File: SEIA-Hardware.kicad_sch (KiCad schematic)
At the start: 1 part, among them IC1 MIMXRT1062DVL6A

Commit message: update 3.10
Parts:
- added IC2: BMF055, BMF055, symbol SEIA_SpecLib:BMF055

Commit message: update on pcb
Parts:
- added IC3: TLV70433DBVEVM-712, SOT95P280X145-5N, symbol SEIA_SpecLib:TLV70433DBVEVM-712
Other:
- note added: "Power"
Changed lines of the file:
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@@
+	)
+	(rectangle
+		(start 29.21 323.85)
+		(end 269.24 393.7)
+		(stroke
+			(width 0.5)
+			(type solid)
+			(color 215 255 101 1)
+		)
+		(fill
+			(type none)
+		)
 	)
 	(rectangle
@@
 		(fill
 			(type none)
+		)
+	)
+	(text "Power"
+		(exclude_from_sim no)
+		(at 39.624 400.05 0)
+		(effects
+			(font
+				(face "Mononoki Nerd Font")
+				(size 5 5)
+			)
 		)
 	)
@@
 					(unit 1)
 				)
+			)
+		)
+	)
+	(symbol
+		(lib_id "SEIA_SpecLib:TLV70433DBVEVM-712")
+		(at 57.15 345.44 0)
+		(unit 1)
+		(exclude_from_sim no)
+		(in_bom yes)
+		(on_board yes)
+		(dnp no)
+		(fields_autoplaced yes)
+		(property "Reference" "IC3"
+			(at 71.12 337.82 0)
+			(effects
+				(font
+					(size 1.27 1.27)
+				)
+			)
+		)
+		(property "Value" "TLV70433DBVEVM-712"
+			(at 71.12 340.36 0)
+			(effects
+				(font
+					(size 1.27 1.27)
+				)
+			)
+		)
+		(property "Footprint" "SOT95P280X145-5N"
+			(at 81.28 342.9 0)
+			(effects
+				(font
+					(size 1.27 1.27)
+				)
+				(justify left)
+				(hide yes)
+			)
+		)
+		(property "Datasheet" "https://componentsearchengine.com/Datasheets/5/TLV70433DBVEVM-712.pdf"
+			(at 81.28 345.44 0)
+			(effects
+				(font
+					(size 1.27 1.27)
+				)
+				(justify left)
+				(hide yes)
+			)
+		)
+		(property "Description" "TEXAS INSTRUMENTS - TLV70433DBVEVM-712 - EVALUATION BOARD, 3.3V, 150mA LDO VOLTAGE REGULATOR"
+			(at 57.15 345.44 0)
+			(effects
+				(font
+					(size 1.27 1.27)
+				)
+				(hide yes)
+			)
+		)
+		(property "Description_1" "TEXAS INSTRUMENTS - TLV70433DBVEVM-712 - EVALUATION BOARD, 3.3V, 150mA LDO VOLTAGE REGULATOR"
+			(at 81.28 347.98 0)
+			(effects
+				(font
+					(size 1.27 1.27)
+				)
+				(justify left)
+				(hide yes)
+			)
+		)
+		(property "Height" "1.45"
+			(at 81.28 350.52 0)
+			(effects
+				(font
+					(size 1.27 1.27)
+				)
+				(justify left)
+				(hide yes)
+			)
+		)
+		(property "Manufacturer_Name" "Texas Instruments"
+			(at 81.28 353.06 0)
+			(effects
+				(font
+					(size 1.27 1.27)
+				)
+				(justify left)
+				(hide yes)
+			)
+		)
+		(property "Manufacturer_Part_Number" "TLV70433DBVEVM-712"
+			(at 81.28 355.6 0)
+			(effects
+				(font
+					(size 1.27 1.27)
+				)
+				(justify left)
+				(hide yes)
+			)
+		)
+		(property "Mouser Part Number" "595-LV70433DBVEVM712"
+			(at 81.28 358.14 0)
+			(effects
+				(font
+					(size 1.27 1.27)
+				)
+				(justify left)
+				(hide yes)
+			)
+		)
+		(property "Mouser Price/Stock" "https://www.mouser.co.uk/ProductDetail/Texas-Instruments/TLV70433DBVEVM-712?qs=TeC8nwD7mVofZYBqOoN1WA%3D%3D"
+			(at 81.28 360.68 0)
+			(effects
+				(font
+					(size 1.27 1.27)
+				)
+				(justify left)
+				(hide yes)
+			)
+		)
+		(property "Arrow Part Number" "TLV70433DBVEVM-712"
+			(at 81.28 363.22 0)
+			(effects
+				(font
+					(size 1.27 1.27)
+				)
+				(justify left)
+				(hide yes)
+			)
+		)
+		(property "Arrow Price/Stock" "null?region=nac"
+			(at 81.28 365.76 0)
+			(effects
+				(font
+					(size 1.27 1.27)
+				)
+				(justify left)
+				(hide yes)
+			)
+		)
+		(pin "2"
+		)
+		(pin "1"
+		)
+		(pin "3"
+		)
+		(pin "5"
+		)
+		(pin "4"
+		)
+		(instances
+			(project ""
+				(path "/10304715-85e0-49b9-9abb-c4d3a396a6f8"
+					(reference "IC3")
+					(unit 1)
+				)

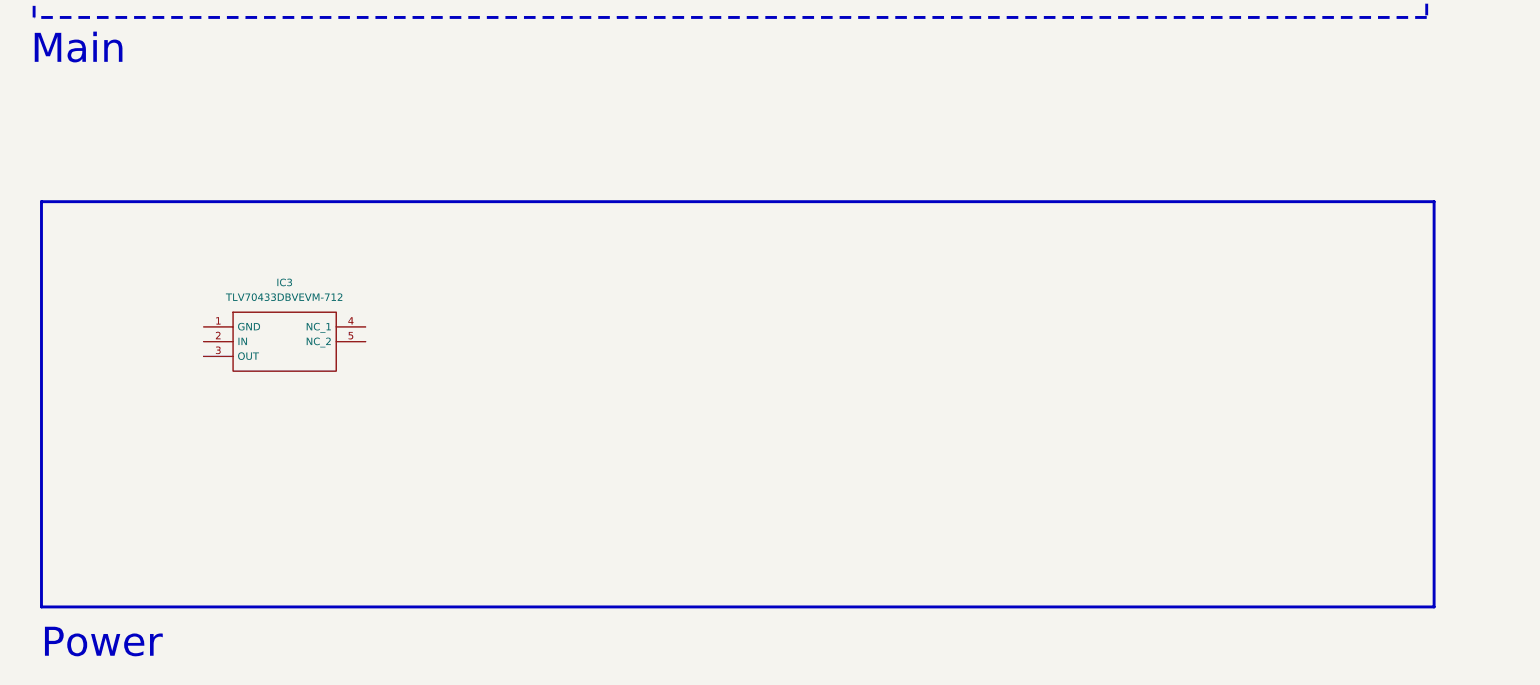
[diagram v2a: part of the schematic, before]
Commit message: added symbols
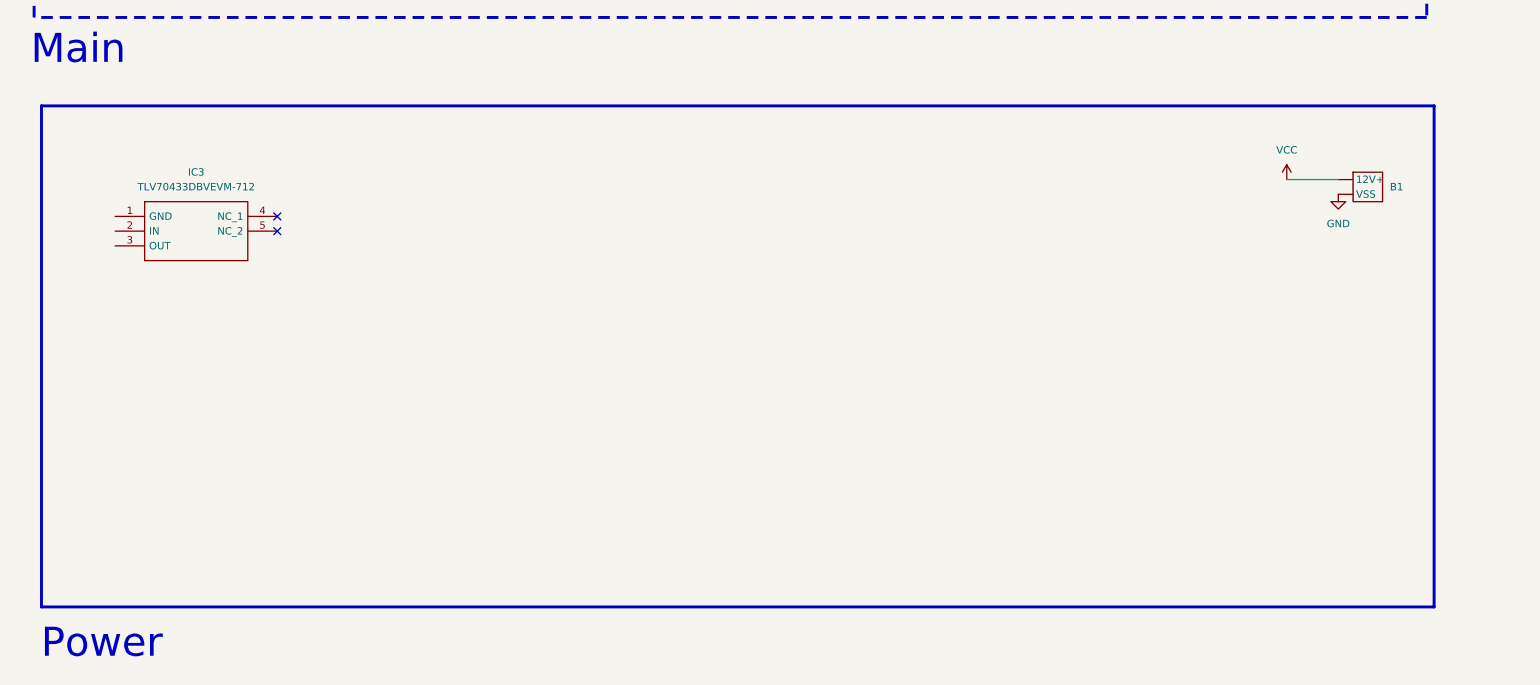
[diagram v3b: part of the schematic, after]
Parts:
- added B1: ~, symbol SEIA_SpecLib:BAT
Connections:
- net GND: now also B1. (VSS)
- new net VCC: B1. (VSS)
- no-connect marks 0 -> 2
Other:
- moved on the sheet: IC3
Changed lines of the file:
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@@
 	)
 	(rectangle
-		(start 29.21 323.85)
+		(start 29.21 307.34)
 		(end 269.24 393.7)
 		(stroke
@@
 		(color 0 0 0 0)
 	)
+	(no_connect
+		(at 69.85 328.93)
+	)
+	(no_connect
+		(at 69.85 326.39)
+	)
 	(wire
 		(pts
@@
 		(pts
 			(xy 31.75 180.34) (xy 50.8 180.34)
+		)
+		(stroke
+			(width 0)
+			(type default)
+		)
+	)
+	(wire
+		(pts
+			(xy 243.84 320.04) (xy 252.73 320.04)
 		)
 		(stroke
@@
 	)
 	(symbol
+		(lib_id "power:VCC")
+		(at 243.84 320.04 0)
+		(unit 1)
+		(exclude_from_sim no)
+		(in_bom yes)
+		(on_board yes)
+		(dnp no)
+		(fields_autoplaced yes)
+		(property "Reference" "#PWR019"
+			(at 243.84 323.85 0)
+			(effects
+				(font
+					(size 1.27 1.27)
+				)
+				(hide yes)
+			)
+		)
+		(property "Value" "VCC"
+			(at 243.84 314.96 0)
+			(effects
+				(font
+					(size 1.27 1.27)
+				)
+			)
+		)
+		(property "Footprint" ""
+			(at 243.84 320.04 0)
+			(effects
+				(font
+					(size 1.27 1.27)
+				)
+				(hide yes)
+			)
+		)
+		(property "Datasheet" ""
+			(at 243.84 320.04 0)
+			(effects
+				(font
+					(size 1.27 1.27)
+				)
+				(hide yes)
+			)
+		)
+		(property "Description" "Power symbol creates a global label with name \"VCC\""
+			(at 243.84 320.04 0)
+			(effects
+				(font
+					(size 1.27 1.27)
+				)
+				(hide yes)
+			)
+		)
+		(pin "1"
+		)
+		(instances
+			(project ""
+				(path "/10304715-85e0-49b9-9abb-c4d3a396a6f8"
+					(reference "#PWR019")
+					(unit 1)
+				)
+			)
+		)
+	)
+	(symbol
 		(lib_id "power:GND")
 		(at 33.02 281.94 0)
@@
 	(symbol
 		(lib_id "SEIA_SpecLib:TLV70433DBVEVM-712")
-		(at 57.15 345.44 0)
+		(at 41.91 326.39 0)
 		(unit 1)
 		(exclude_from_sim no)
@@
 		(fields_autoplaced yes)
 		(property "Reference" "IC3"
-			(at 71.12 337.82 0)
+			(at 55.88 318.77 0)
 			(effects
 				(font
@@
 		)
 		(property "Value" "TLV70433DBVEVM-712"
-			(at 71.12 340.36 0)
+			(at 55.88 321.31 0)
 			(effects
 				(font
@@
 		)
 		(property "Footprint" "SOT95P280X145-5N"
-			(at 81.28 342.9 0)
+			(at 66.04 323.85 0)
 			(effects
 				(font
@@
 		)
 		(property "Datasheet" "https://componentsearchengine.com/Datasheets/5/TLV70433DBVEVM-712.pdf"
-			(at 81.28 345.44 0)
+			(at 66.04 326.39 0)
 			(effects
 				(font
@@
 		)
 		(property "Description" "TEXAS INSTRUMENTS - TLV70433DBVEVM-712 - EVALUATION BOARD, 3.3V, 150mA LDO VOLTAGE REGULATOR"
-			(at 57.15 345.44 0)
+			(at 41.91 326.39 0)
 			(effects
 				(font
@@
 		)
 		(property "Description_1" "TEXAS INSTRUMENTS - TLV70433DBVEVM-712 - EVALUATION BOARD, 3.3V, 150mA LDO VOLTAGE REGULATOR"
-			(at 81.28 347.98 0)
+			(at 66.04 328.93 0)
 			(effects
 				(font
@@
 		)
 		(property "Height" "1.45"
-			(at 81.28 350.52 0)
+			(at 66.04 331.47 0)
 			(effects
 				(font
@@
 		)
 		(property "Manufacturer_Name" "Texas Instruments"
-			(at 81.28 353.06 0)
+			(at 66.04 334.01 0)
 			(effects
 				(font
@@
 		)
 		(property "Manufacturer_Part_Number" "TLV70433DBVEVM-712"
-			(at 81.28 355.6 0)
+			(at 66.04 336.55 0)
 			(effects
 				(font
@@
 		)
 		(property "Mouser Part Number" "595-LV70433DBVEVM712"
-			(at 81.28 358.14 0)
+			(at 66.04 339.09 0)
 			(effects
 				(font
@@
 		)
 		(property "Mouser Price/Stock" "https://www.mouser.co.uk/ProductDetail/Texas-Instruments/TLV70433DBVEVM-712?qs=TeC8nwD7mVofZYBqOoN1WA%3D%3D"
-			(at 81.28 360.68 0)
+			(at 66.04 341.63 0)
 			(effects
 				(font
@@
 		)
 		(property "Arrow Part Number" "TLV70433DBVEVM-712"
-			(at 81.28 363.22 0)
+			(at 66.04 344.17 0)
 			(effects
 				(font
@@
 		)
 		(property "Arrow Price/Stock" "null?region=nac"
-			(at 81.28 365.76 0)
+			(at 66.04 346.71 0)
 			(effects
 				(font
@@
 					(unit 1)
 				)
+			)
+		)
+	)
+	(symbol
+		(lib_id "SEIA_SpecLib:BAT")
+		(at 256.54 325.12 0)
+		(unit 1)
+		(exclude_from_sim no)
+		(in_bom yes)
+		(on_board yes)
+		(dnp no)
+		(fields_autoplaced yes)
+		(property "Reference" "B1"
+			(at 261.62 321.3099 0)
+			(effects
+				(font
+					(size 1.27 1.27)
+				)
+				(justify left)
+			)
+		)
+		(property "Value" "~"
+			(at 261.62 322.58 0)
+			(effects
+				(font
+					(size 1.27 1.27)
+				)
+				(justify left)
+			)
+		)
+		(property "Footprint" ""
+			(at 256.54 325.12 0)
+			(effects
+				(font
+					(size 1.27 1.27)
+				)
+				(hide yes)
+			)
+		)
+		(property "Datasheet" ""
+			(at 256.54 325.12 0)
+			(effects
+				(font
+					(size 1.27 1.27)
+				)
+				(hide yes)
+			)
+		)
+		(property "Description" ""
+			(at 256.54 325.12 0)
+			(effects
+				(font
+					(size 1.27 1.27)
+				)
+				(hide yes)
+			)
+		)
+		(pin ""
+		)
+		(pin ""
+		)
+		(instances
+			(project ""
+				(path "/10304715-85e0-49b9-9abb-c4d3a396a6f8"
+					(reference "B1")
+					(unit 1)
+				)
+			)
+		)
+	)
+	(symbol
+		(lib_id "power:GND")
+		(at 252.73 322.58 0)
+		(unit 1)
+		(exclude_from_sim no)
+		(in_bom yes)
+		(on_board yes)
+		(dnp no)
+		(fields_autoplaced yes)
+		(property "Reference" "#PWR020"
+			(at 252.73 328.93 0)
+			(effects
+				(font
+					(size 1.27 1.27)
+				)
+				(hide yes)
+			)
+		)
+		(property "Value" "GND"
+			(at 252.73 327.66 0)
+			(effects
+				(font
+					(size 1.27 1.27)
+				)
+			)
+		)
+		(property "Footprint" ""
+			(at 252.73 322.58 0)
+			(effects
+				(font
+					(size 1.27 1.27)
+				)
+				(hide yes)
+			)
+		)
+		(property "Datasheet" ""
+			(at 252.73 322.58 0)
+			(effects
+				(font
+					(size 1.27 1.27)
+				)
+				(hide yes)
+			)
+		)
+		(property "Description" "Power symbol creates a global label with name \"GND\" , ground"
+			(at 252.73 322.58 0)
+			(effects
+				(font
+					(size 1.27 1.27)
+				)
+				(hide yes)
+			)
+		)
+		(pin "1"
+		)
+		(instances
+			(project ""
+				(path "/10304715-85e0-49b9-9abb-c4d3a396a6f8"
+					(reference "#PWR020")
+					(unit 1)
+				)

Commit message: BNO055 Wired
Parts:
- removed IC3: TLV70433DBVEVM-712, SOT95P280X145-5N, symbol SEIA_SpecLib:TLV70433DBVEVM-712
- added C1, C2: CL21A475KAQNNNE, CAPC2012X140N, symbol SEIA_SpecLib:CL21A475KAQNNNE
- added C3, C6: C0603C220J5GACTU, CAPC1608X87N, symbol SEIA_SpecLib:C0603C220J5GACTU
- added C4, C5: CL05B104KP5NNNC, CAPC1005X55N, symbol SEIA_SpecLib:CL05B104KP5NNNC
- added PS1: TLV70433DBVR, SOT95P280X145-5N, symbol SEIA_SpecLib:TLV70433DBVR
- added RN1: EXB28V103JX, EXB28V510JX, symbol SEIA_SpecLib:EXB28V103JX
- added Y1: XRCGB32M768F2N10R0, XRCGB, symbol SEIA_SpecLib:XRCGB32M768F2N10R0
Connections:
- net GND: now also IC2.10 (PA28), IC2.15 (PA23), IC2.16 (PA22), IC2.2 (GND), IC2.25 (GNDIO), C1.2, C2.2, C3.2, C4.1, C5.2, C6.1, PS1.1 (GND), RN1.1, RN1.2, RN1.3
- net VCC: now also C1.1, PS1.2 (IN)
- net I2C_Addr: now reaches IC2.23 (PA17)
- net I2C_Addr: now also RN1.6
- net C_In: now reaches IC2.26 (PA01)
- net C_In: now also C6.2, Y1.3 (XTAL_2)
- net C_Out: now reaches IC2.27 (PA00)
- net C_Out: now also C3.1, Y1.1 (XTAL_1)
- net +3V3: now reaches IC2.28 (VDDIO)
- net +3V3: now also IC2.3 (VDD), IC2.4 (PB02), C2.1, C4.2, PS1.3 (OUT)
- net MOSP1: now reaches IC2.5 (PB01)
- net MOSP1: now also RN1.8
- net MOSP2: now reaches IC2.6 (PB00)
- net MOSP2: now also RN1.7
- net at IC2.9 (CAP): now also C5.1
- no-connect marks 2 -> 5

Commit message: Update: Imported necessary library to transfter to teensy
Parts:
- added LS1: PKMCS0909E4000-R1, PKMCS0909E4000R1, symbol SEIA_SpecLib:PKMCS0909E4000-R1
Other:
- note removed: "Main"
- note removed: "Power"
- moved on the sheet: B1, C1, C2, C3, C4, C5, C6, IC2, PS1, RN1, Y1

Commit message: new stuff
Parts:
- added IC3: BMP390, BMP390, symbol SEIA_SpecLib:BMP390
- added IC4: DP83825IRMQR, DP83825IRMQR, symbol SEIA_SpecLib:DP83825IRMQR
- added IC6: MKL02Z32VFG4, QFN50P300X300X65-17N-D, symbol SEIA_SpecLib:MKL02Z32VFG4
- added J1: ST1W008S4TR2000, ST1W008S4TR2000:JAE_ST1W008S4TR2000, symbol SEIA_SpecLib:ST1W008S4TR2000
- added Q1: DMG2305UX, SOT96P240X115-3N, symbol SEIA_SpecLib:DMG2305UX
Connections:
- new net: J1.GND1 (GND), J1.GND2 (GND), J1.GND3 (GND), J1.GND4 (GND)
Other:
- moved on the sheet: C3, C4, C5, C6, IC2, LS1, RN1, Y1

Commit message: patched and upgraded spec
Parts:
- added C7, C8: CL05B104KP5NNNC, CAPC1005X55N, symbol SEIA_SpecLib:CL05B104KP5NNNC
- added R1, R2: ERJ-2GEJ472X, RESC1005X40N, symbol SEIA_SpecLib:ERJ-2GEJ472X
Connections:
- net +3V3: now also IC3.1 (VDDIO), IC3.10 (VDD), IC3.6 (CSB), C7.1, C8.2, R1.2, R2.1
- net GND: now also IC3.3 (VSS_1), IC3.5 (SDO), IC3.8 (VSS_2), IC3.9 (VSS_3), C7.2, C8.1
- net BAR_SCK: now reaches IC3.2 (SCK)
- net BAR_SCK: now also R2.2
- net BAR_SDA: now reaches IC3.4 (SDI)
- net BAR_SDA: now also R1.1
- no-connect marks 5 -> 6
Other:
- company: InLabs -> InLabs - Designed by Ren
- moved on the sheet: B1, C1, C2, C3, C4, C5, C6, IC1, IC2, IC3, IC4, IC6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
